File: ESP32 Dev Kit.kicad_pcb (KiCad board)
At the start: 2 copper layers, 24 parts, among them J1 USB_B_Micro, J2 Conn_01x15, J3 Conn_01x15, Q1 2N2222, Q2 2N2222, SW1 SW_Push, SW2 SW_Push, U1 AMS1117-3.3, U2 CH340C, U3 ESP32-WROOM-32

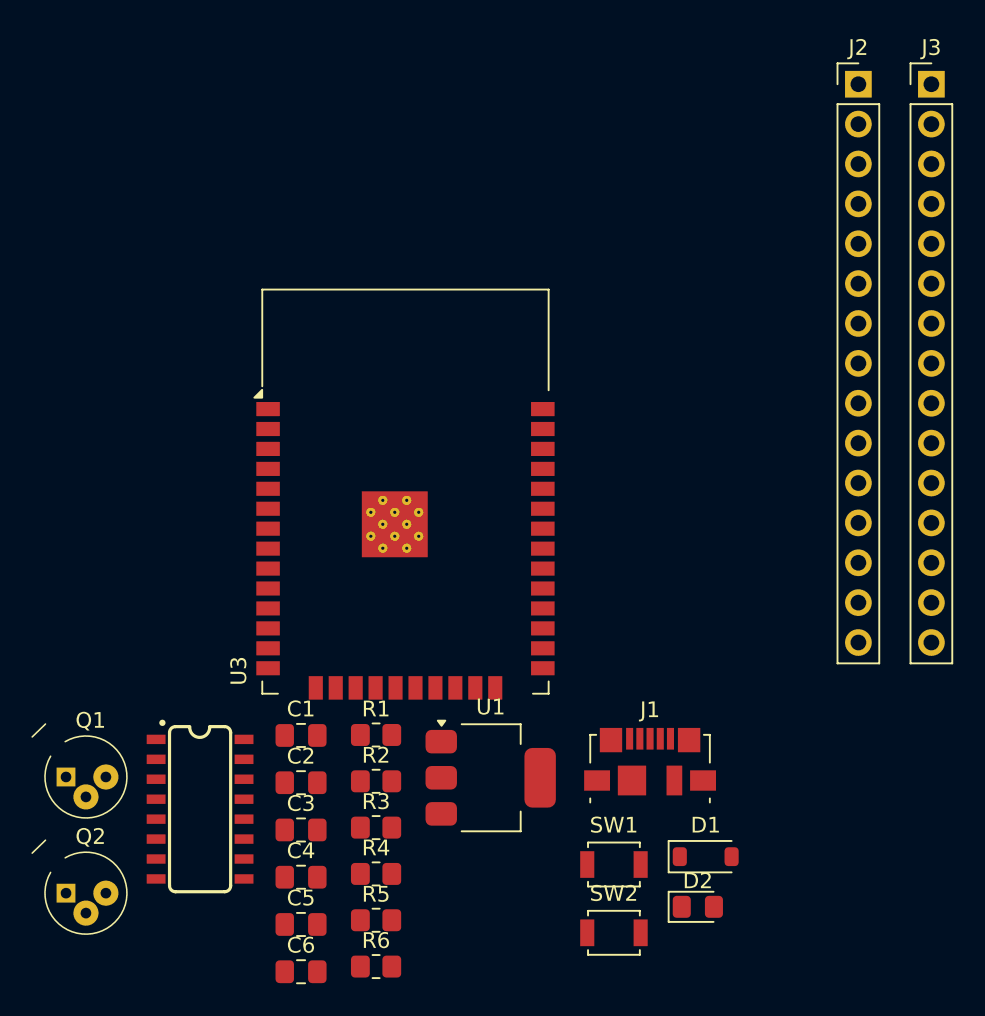
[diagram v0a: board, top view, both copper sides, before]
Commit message: Footprints placed & Revised
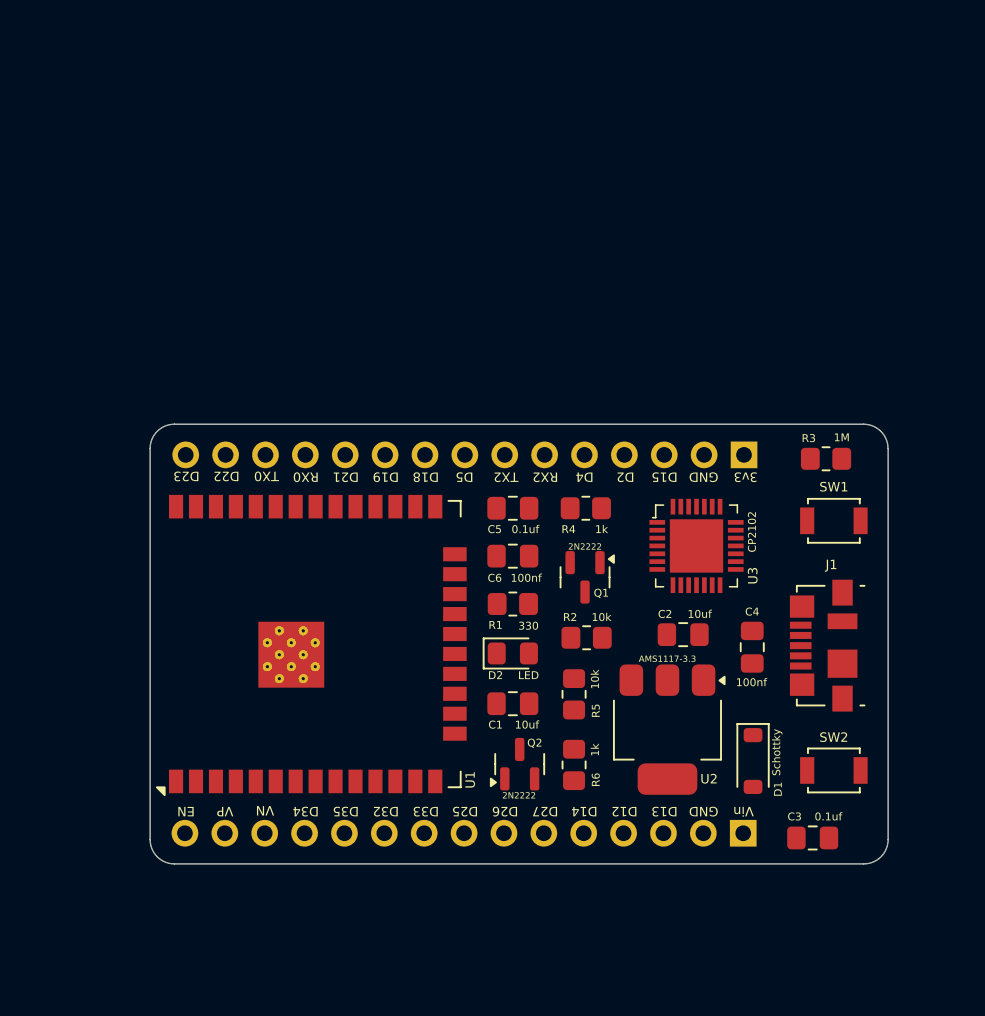
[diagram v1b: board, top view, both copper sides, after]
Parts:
- removed the U2 at (129.8, 116.8)
- added U3: CP2102-GMR_NRND, digikey-footprints:VFQFN-28-1EP_5x5mm, F.Cu at (161.4, 100.0)
- J2, J3: moved to B.Cu
- Q1, Q2: footprint digikey-footprints:TO-18-3 -> Package_TO_SOT_SMD:SOT-23
- moved J3 49.2 mm to (164.4, 118.3), turned to 90 degrees
- moved R3 37.1 mm to (169.7, 94.5)
- moved Q1 35.4 mm to (154.3, 102.0), turned to -90 degrees
- moved C3 32.6 mm to (168.8, 118.6)
- moved C4 32.3 mm to (165.0, 106.5), turned to 90 degrees
- moved Q2 30.0 mm to (150.2, 113.9), turned to 90 degrees
- moved C5 29.7 mm to (149.8, 97.6), turned to 180 degrees
- moved C6 29.7 mm to (149.8, 100.7), turned to 180 degrees
- moved R4 26.9 mm to (154.4, 97.6), turned to 180 degrees
- moved C2 26.1 mm to (160.6, 105.7)
- moved SW1 26.0 mm to (170.2, 98.4)
- moved J2 24.7 mm to (164.5, 94.2), turned to 90 degrees
- moved D2 20.0 mm to (149.8, 106.8)
- moved R5 19.1 mm to (153.7, 109.5), turned to -90 degrees
- moved R6 18.0 mm to (153.7, 114.0), turned to -90 degrees
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- renumbered U3 to U1, U1 to U2
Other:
- board outline added: 47 x 28 mm
- board text added: "0.1uf"
- board text added: "100nf"
- board text added: "10k"
- board text added: "10uf"
- board text added: "1M"
- board text added: "1k"
- board text added: "2N2222"
- board text added: "330"
- board text added: "3v3"
- board text added: "AMS1117-3.3"
- board text added: "CP2102"
- board text added: "D12"
- board text added: "D13"
- board text added: "D14"
- board text added: "D15"
- board text added: "D18"
- board text added: "D19"
- board text added: "D2"
- board text added: "D21"
- board text added: "D22"
- board text added: "D23"
- board text added: "D25"
- board text added: "D26"
- board text added: "D27"
- board text added: "D32"
- board text added: "D33"
- board text added: "D34"
- board text added: "D35"
- board text added: "D4"
- board text added: "D5"
- board text added: "EN"
- board text added: "GND"
- board text added: "LED"
- board text added: "RX0"
- board text added: "RX2"
- board text added: "Schottky"
- board text added: "TX0"
- board text added: "TX2"
- board text added: "VN"
- board text added: "VP"
- board text added: "Vin"

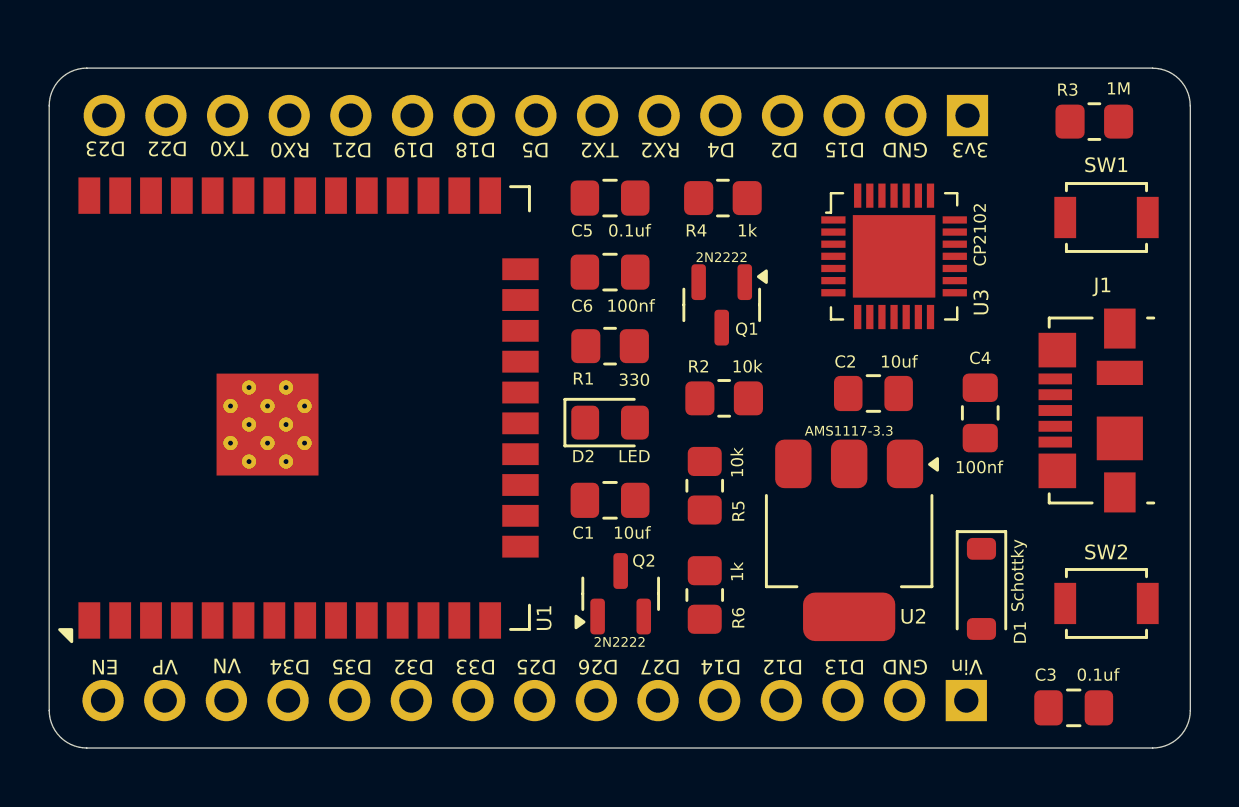
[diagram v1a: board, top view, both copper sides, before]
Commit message: Added Traces to the PCB - R1
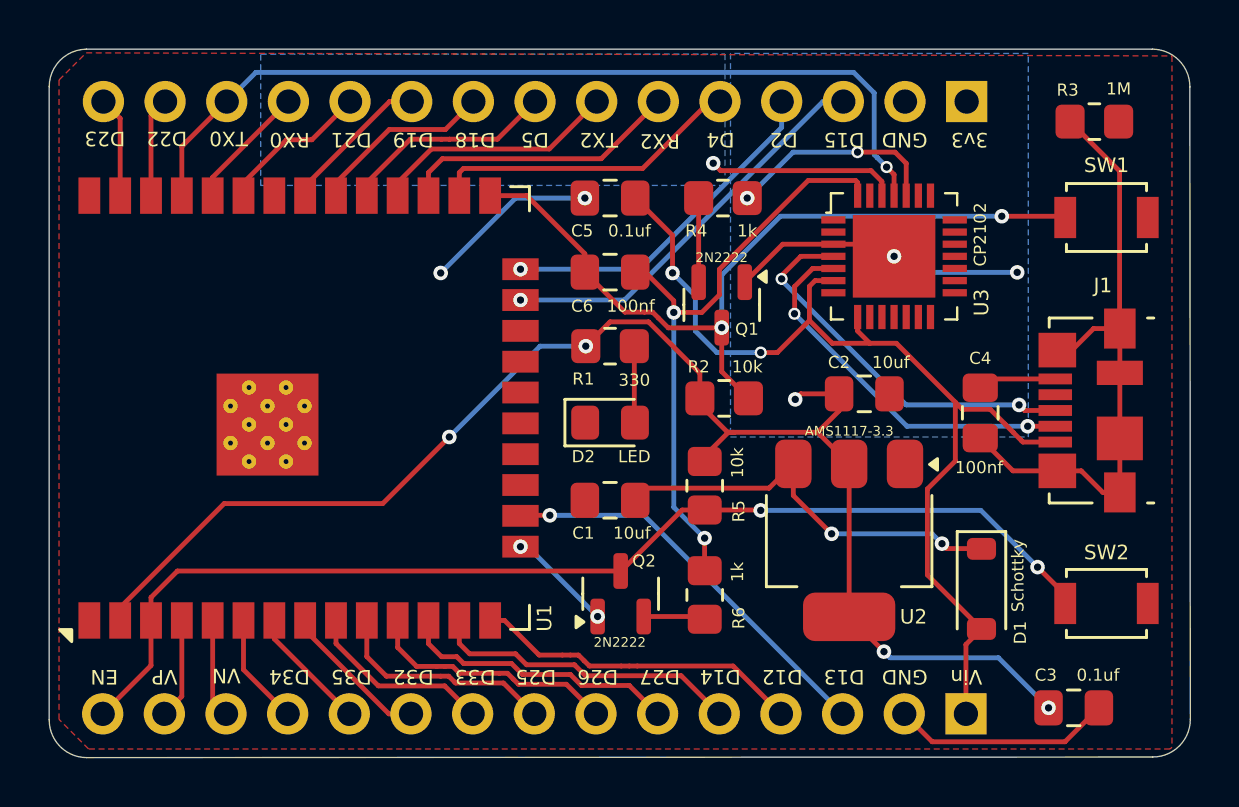
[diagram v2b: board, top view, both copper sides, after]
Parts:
- moved J2 0.58 mm to (164.4, 93.6)
- moved J3 0.55 mm to (164.4, 118.8)
- moved C2 0.38 mm to (160.2, 105.7)
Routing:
- net /3.3v: track 0.00 -> 60.3 mm, vias 0 -> 5
- net /EN: track 0.00 -> 46.6 mm, vias 0 -> 2
- net /5v: track 0.00 -> 42.6 mm, vias 0 -> 2
- net /TX0: track 0.00 -> 36.7 mm, vias 0 -> 1
- net GND: track 0.00 -> 36.3 mm, vias 0 -> 6
- net /Boot: track 0.00 -> 32.9 mm, vias 0 -> 2
- net Net-(J1-Shield): track 0.00 -> 25.7 mm
- net /DTR: track 0.00 -> 24.7 mm, vias 0 -> 2
- net Net-(D1-K): track 0.00 -> 17.1 mm, vias 0 -> 2
- net /D15: track 0.00 -> 16.7 mm, vias 0 -> 1
- net /D13: track 0.00 -> 16.7 mm, vias 0 -> 1
- net Net-(J1-D+): track 0.00 -> 16.2 mm, vias 0 -> 2
- net Net-(J1-D-): track 0.00 -> 15.7 mm, vias 0 -> 2
- net /D2: track 0.00 -> 14.2 mm, vias 0 -> 1
- net /D12: track 0.00 -> 13.6 mm
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- added copper zone on B.Cu, net /3.3v
- added copper zone on B.Cu, net /RX0
- added copper zone on F.Cu, net GND
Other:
- board size 47 x 28 mm -> 47 x 29.2 mm

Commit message: PCB Revised
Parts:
- added G***: LOGO, Brij:Brij Logo, B.Cu at (136.9, 100.7)
- added REF**: KiCad-Logo2_5mm_SilkScreen, Symbol:KiCad-Logo2_5mm_SilkScreen, B.Cu at (161.8, 112.6)
- moved C5 28.9 mm to (169.6, 118.6), turned to 0 degrees
- moved C3 19.1 mm to (150.1, 115.2), turned to 180 degrees
- moved R3 11.5 mm to (165.3, 105.0), turned to -90 degrees
- moved C2 11.0 mm to (154.8, 115.3), turned to 180 degrees
- moved D1 9.61 mm to (160.7, 105.2), turned to 0 degrees
- moved R1 8.70 mm to (150.1, 112.4), turned to 180 degrees
- moved C4 7.61 mm to (165.8, 98.9)
- moved C1 7.03 mm to (154.9, 105.2)
- moved Q2 6.68 mm to (154.8, 109.1)
- moved R2 6.15 mm to (149.9, 101.7), turned to 90 degrees
- moved R6 5.45 mm to (151.6, 108.9)
- moved R5 3.36 mm to (154.8, 112.6), turned to 180 degrees
- moved C6 3.35 mm to (149.9, 97.3)
- moved D2 2.24 mm to (148.9, 108.9), turned to -90 degrees
- moved U2 1.27 mm to (160.9, 111.7)
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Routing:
- net GND: track 36.3 -> 64.4 mm, vias 6 -> 9
- net /5v: track 42.6 -> 30.7 mm
- net /RX0: track 13.0 -> 24.9 mm, vias 1 -> 2
- net Net-(D1-K): track 17.1 -> 6.71 mm, vias 2 -> 0
- net Net-(J1-D+): track 16.2 -> 9.43 mm, vias 2 -> 0
- net Net-(J1-D-): track 15.7 -> 9.52 mm
- net Net-(Q2-B): track 2.56 -> 8.58 mm
- net /RTS: track 8.86 -> 3.21 mm, vias 2 -> 0
- net /TX0: track 36.7 -> 31.8 mm
- net /Boot: track 32.9 -> 29.6 mm
- net /D13: track 16.7 -> 19.2 mm, vias 1 -> 0
- net /EN: track 46.6 -> 49.0 mm, vias 2 -> 3
- net /3.3v: track 60.3 -> 58.1 mm, vias 5 -> 4
- net Net-(J1-Shield): track 25.7 -> 28.0 mm
- net /DTR: track 24.7 -> 23.0 mm, vias 2 -> 0
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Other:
- board text added: "Boot"
- board text added: "ESP32 Dev Kit"
- board text added: "ESP32-WROOM-32"

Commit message: Final PCB
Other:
- board text removed: "LED"
